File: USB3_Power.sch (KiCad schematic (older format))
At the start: 42 parts, among them U4 NCP1117ST33T3G, U6 CYUSB3014-BZXI

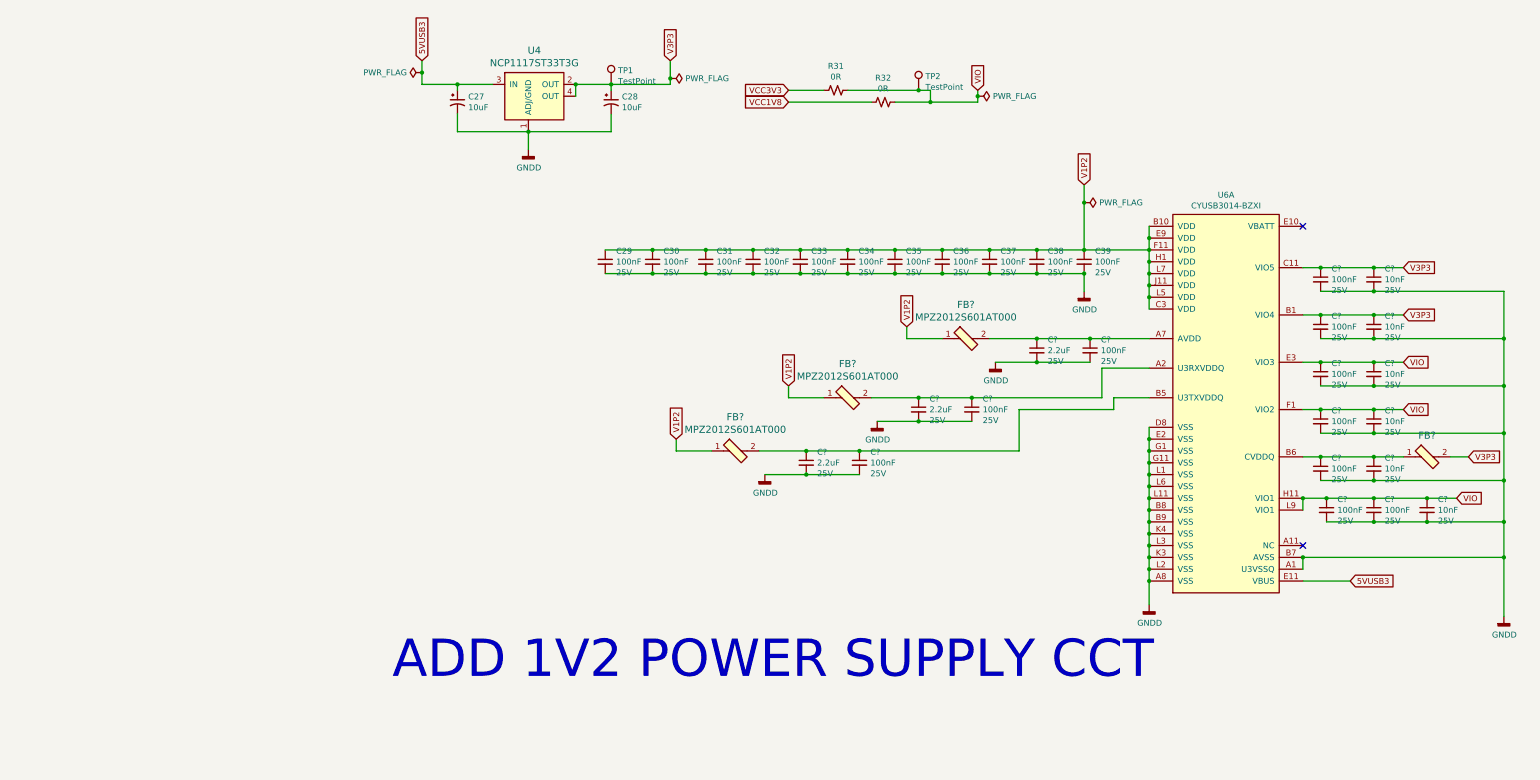
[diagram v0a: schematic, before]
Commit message: Completed USB3 1.2V Added 5V regulator cct partially completed Added BTB connector
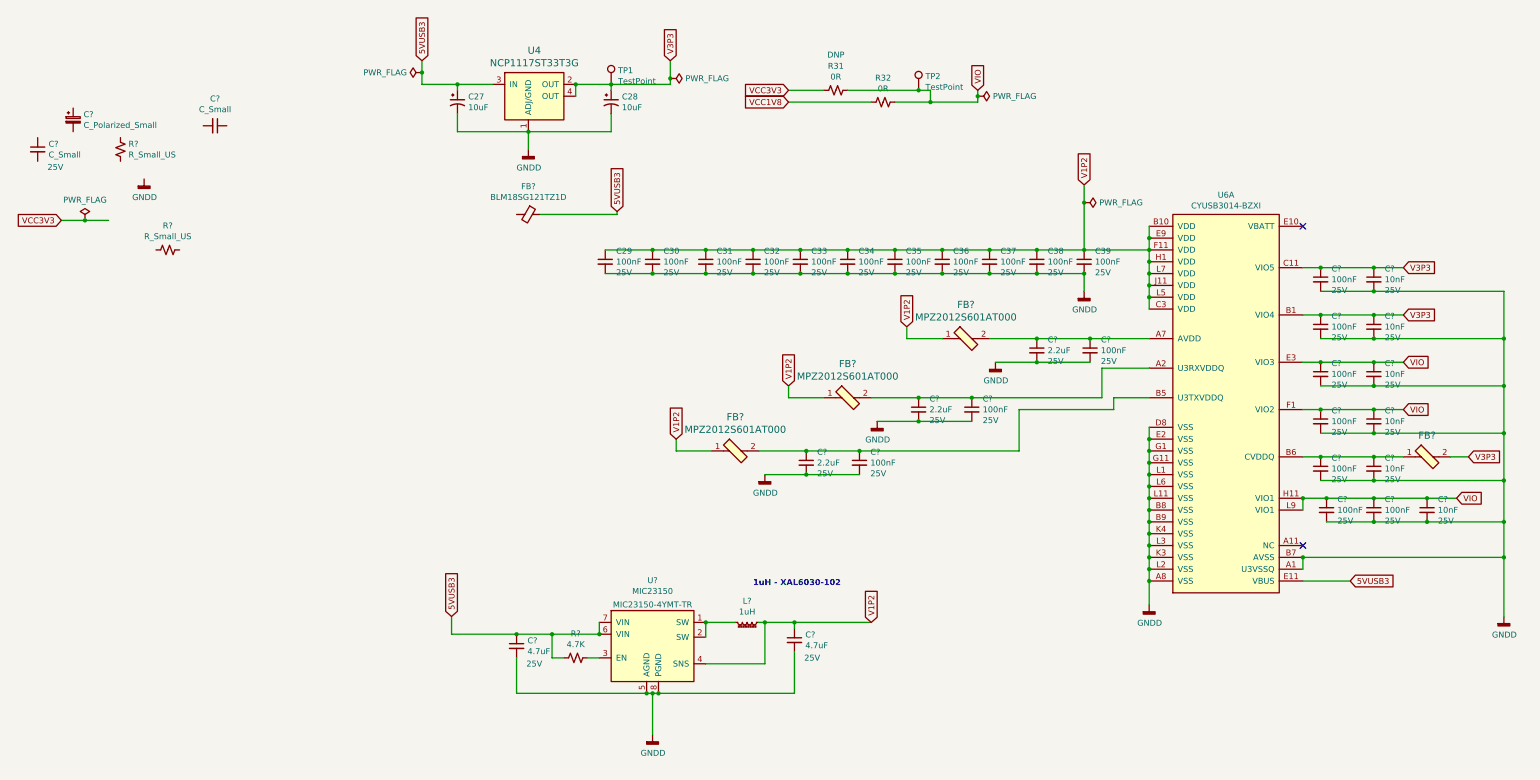
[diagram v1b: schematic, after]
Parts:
- added C?: C_Small, Capacitor_SMD:C_0603_1608Metric_Pad1.08x0.95mm_HandSolder, symbol Device:C_Small
- added C?: C_Polarized_Small, Capacitor_Tantalum_SMD:CP_EIA-1608-10_AVX-L_Pad1.25x1.05mm_HandSolder, symbol Device:C_Polarized_Small
- added C?: C_Small, symbol Device:C_Small
- added C? (x2): 4.7uF, Capacitor_SMD:C_0603_1608Metric_Pad1.08x0.95mm_HandSolder, symbol Device:C_Small
- added FB?: BLM18SG121TZ1D, Inductor_SMD:L_0603_1608Metric_Pad1.05x0.95mm_HandSolder, symbol Device:FerriteBead_Small
- added L?: 1uH, symbol Device:L_Ferrite_Small
- added R? (x2): R_Small_US, Resistor_SMD:R_0603_1608Metric_Pad0.98x0.95mm_HandSolder, symbol Device:R_Small_US
- added R?: 4.7K, Resistor_SMD:R_0603_1608Metric_Pad0.98x0.95mm_HandSolder, symbol Device:R_Small_US
- added U?: MIC23150, GM_TDFN:TDFN-8-2x2mm_P0.5mm, symbol GM_Voltage_Regulators:MIC23150
- R31: DNP (none) -> DNP
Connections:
- net 5VUSB3: now also C?.1, FB?.1, R?.2, U?.6 (VIN), U?.7 (VIN)
- net GNDD: now also C?.2, C?.2, U?.5 (AGND), U?.8 (PGND)
- net V1P2: now also C?.1, L?.1, U?.4 (SNS)
- new net: L?.2, U?.1 (SW), U?.2 (SW)
- new net: R?.1, U?.3 (EN)
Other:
- note added: "1uH - XAL6030-102"
- note removed: "ADD 1V2 POWER SUPPLY CCT"

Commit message: Added USB3 SRAM Added 5V regulator
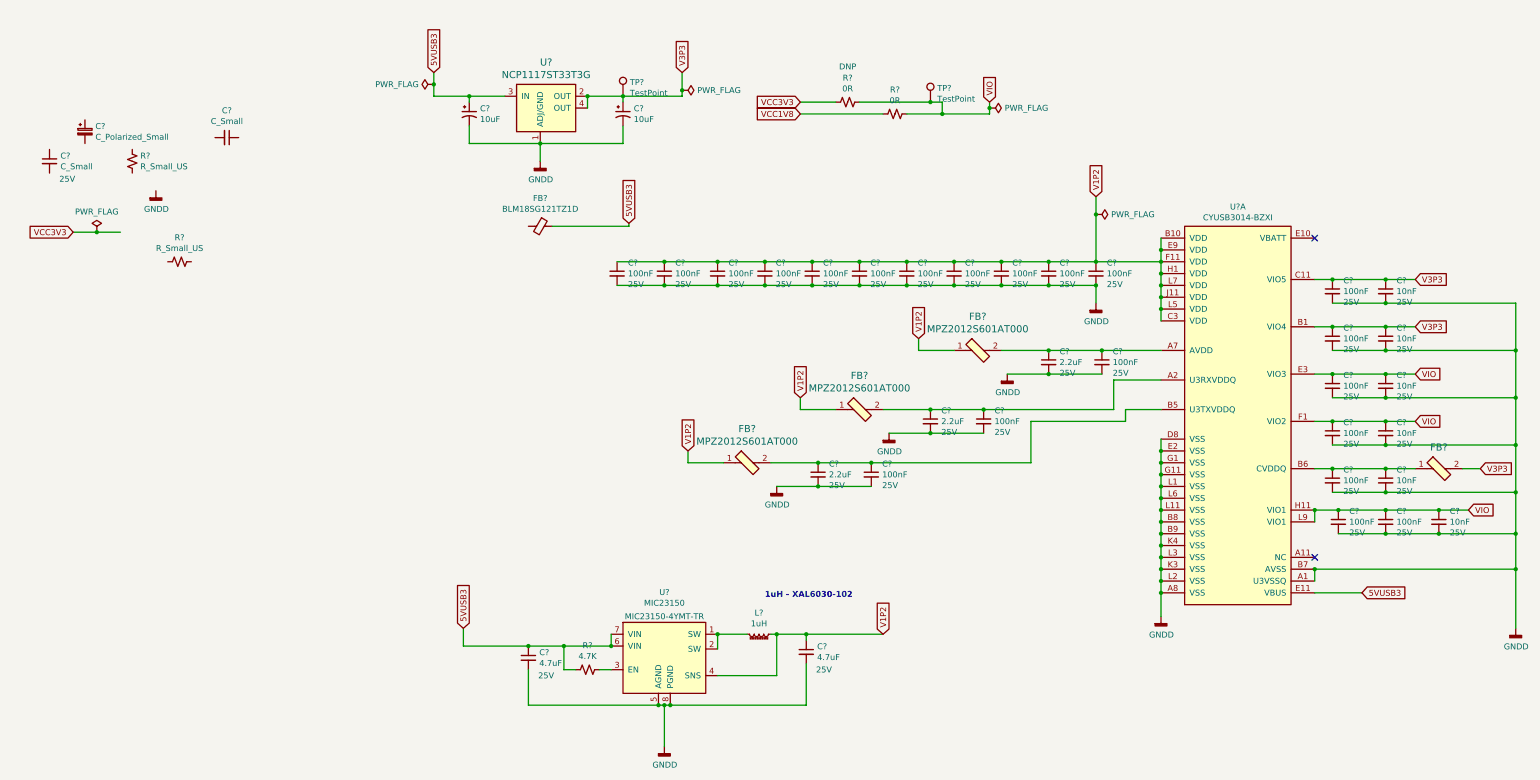
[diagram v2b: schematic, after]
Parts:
- removed C27, C28: 10uF, Capacitor_Tantalum_SMD:CP_EIA-3528-21_Kemet-B_Pad1.50x2.35mm_HandSolder, symbol Device:C_Polarized_Small_US
- removed C29, C30, C31, C32, C33, C34, C35, C36, C37, C38, C39, C? (x10): 100nF, Capacitor_SMD:C_0603_1608Metric_Pad1.08x0.95mm_HandSolder, symbol Device:C_Small
- removed C? (x3): 2.2uF, Capacitor_SMD:C_0603_1608Metric_Pad1.08x0.95mm_HandSolder, symbol Device:C_Small
- removed C? (x6): 10nF, Capacitor_SMD:C_0603_1608Metric_Pad1.08x0.95mm_HandSolder, symbol Device:C_Small
- removed C?: C_Small, Capacitor_SMD:C_0603_1608Metric_Pad1.08x0.95mm_HandSolder, symbol Device:C_Small
- removed C?: C_Polarized_Small, Capacitor_Tantalum_SMD:CP_EIA-1608-10_AVX-L_Pad1.25x1.05mm_HandSolder, symbol Device:C_Polarized_Small
- removed C?: C_Small, symbol Device:C_Small
- removed C? (x2): 4.7uF, Capacitor_SMD:C_0603_1608Metric_Pad1.08x0.95mm_HandSolder, symbol Device:C_Small
- removed FB? (x4): MPZ2012S601AT000, digikey-footprints:0805, symbol dk_Ferrite-Beads-and-Chips:MPZ2012S601AT000
- removed FB?: BLM18SG121TZ1D, Inductor_SMD:L_0603_1608Metric_Pad1.05x0.95mm_HandSolder, symbol Device:FerriteBead_Small
- removed L?: 1uH, symbol Device:L_Ferrite_Small
- removed R31, R32: 0R, Resistor_SMD:R_0603_1608Metric_Pad0.98x0.95mm_HandSolder, symbol Device:R_Small_US
- removed R? (x2): R_Small_US, Resistor_SMD:R_0603_1608Metric_Pad0.98x0.95mm_HandSolder, symbol Device:R_Small_US
- removed R?: 4.7K, Resistor_SMD:R_0603_1608Metric_Pad0.98x0.95mm_HandSolder, symbol Device:R_Small_US
- removed TP1, TP2: TestPoint, TestPoint:TestPoint_Pad_2.0x2.0mm, symbol Connector:TestPoint
- removed U4: NCP1117ST33T3G, digikey-footprints:SOT-223, symbol dk_PMIC-Voltage-Regulators-Linear:NCP1117ST33T3G
- removed U6: CYUSB3014-BZXI, Package_BGA:BGA121C80P11X11_1000X1000X120, symbol GM_Microcontrollers:CYUSB3014-BZXI
- removed U?: MIC23150, GM_TDFN:TDFN-8-2x2mm_P0.5mm, symbol GM_Voltage_Regulators:MIC23150
- added C? (x2): 4.7uF, Capacitor_SMD:C_0603_1608Metric_Pad1.08x0.95mm_HandSolder, symbol Device:C_Small
- added C?: C_Small, symbol Device:C_Small
- added C?: C_Polarized_Small, Capacitor_Tantalum_SMD:CP_EIA-1608-10_AVX-L_Pad1.25x1.05mm_HandSolder, symbol Device:C_Polarized_Small
- added C?: C_Small, Capacitor_SMD:C_0603_1608Metric_Pad1.08x0.95mm_HandSolder, symbol Device:C_Small
- added C? (x21): 100nF, Capacitor_SMD:C_0603_1608Metric_Pad1.08x0.95mm_HandSolder, symbol Device:C_Small
- added C? (x6): 10nF, Capacitor_SMD:C_0603_1608Metric_Pad1.08x0.95mm_HandSolder, symbol Device:C_Small
- added C? (x3): 2.2uF, Capacitor_SMD:C_0603_1608Metric_Pad1.08x0.95mm_HandSolder, symbol Device:C_Small
- added C? (x2): 10uF, Capacitor_Tantalum_SMD:CP_EIA-3528-21_Kemet-B_Pad1.50x2.35mm_HandSolder, symbol Device:C_Polarized_Small_US
- added FB?: BLM18SG121TZ1D, Inductor_SMD:L_0603_1608Metric_Pad1.05x0.95mm_HandSolder, symbol Device:FerriteBead_Small
- added FB? (x4): MPZ2012S601AT000, digikey-footprints:0805, symbol dk_Ferrite-Beads-and-Chips:MPZ2012S601AT000
- added L?: 1uH, symbol Device:L_Ferrite_Small
- added R?: 4.7K, Resistor_SMD:R_0603_1608Metric_Pad0.98x0.95mm_HandSolder, symbol Device:R_Small_US
- added R? (x2): R_Small_US, Resistor_SMD:R_0603_1608Metric_Pad0.98x0.95mm_HandSolder, symbol Device:R_Small_US
- added R? (x2): 0R, Resistor_SMD:R_0603_1608Metric_Pad0.98x0.95mm_HandSolder, symbol Device:R_Small_US
- added TP? (x2): TestPoint, TestPoint:TestPoint_Pad_2.0x2.0mm, symbol Connector:TestPoint
- added U?: MIC23150, GM_TDFN:TDFN-8-2x2mm_P0.5mm, symbol GM_Voltage_Regulators:MIC23150
- added U?: NCP1117ST33T3G, digikey-footprints:SOT-223, symbol dk_PMIC-Voltage-Regulators-Linear:NCP1117ST33T3G
- added U?: CYUSB3014-BZXI, Package_BGA:BGA121C80P11X11_1000X1000X120, symbol GM_Microcontrollers:CYUSB3014-BZXI
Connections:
- net 5VUSB3: now also C?.1, C?.1, FB?.1, R?.2, U?.3 (IN), U?.6 (VIN), U?.7 (VIN), U?.E11 (VBUS)
- net GNDD: now also C?.2, C?.2, C?.2, C?.2, C?.2, C?.2, C?.2, C?.2, C?.2, C?.2, C?.2, C?.2, C?.2, C?.2, C?.2, C?.2, C?.2, C?.2, C?.2, C?.2, C?.2, C?.2, C?.2, C?.2, C?.2, C?.2, C?.2, C?.2, C?.2, C?.2, C?.2, C?.2, C?.2, C?.2, U?.1 (ADJ/GND), U?.5 (AGND), U?.8 (PGND), U?.A1 (U3VSSQ), U?.A8 (VSS), U?.B7 (AVSS), U?.B8 (VSS), U?.B9 (VSS), U?.D8 (VSS), U?.E2 (VSS), U?.G1 (VSS), U?.G11 (VSS), U?.K3 (VSS), U?.K4 (VSS), U?.L1 (VSS), U?.L11 (VSS), U?.L2 (VSS), U?.L3 (VSS), U?.L6 (VSS)
- net V1P2: now also C?.1, C?.1, C?.1, C?.1, C?.1, C?.1, C?.1, C?.1, C?.1, C?.1, C?.1, C?.1, FB?.1, FB?.1, FB?.1, L?.1, U?.4 (SNS), U?.B10 (VDD), U?.C3 (VDD), U?.E9 (VDD), U?.F11 (VDD), U?.H1 (VDD), U?.J11 (VDD), U?.L5 (VDD), U?.L7 (VDD)
- net V3P3: now also C?.1, C?.1, C?.1, C?.1, C?.1, FB?.2, TP?.1, U?.2 (OUT), U?.4 (OUT), U?.B1 (VIO4), U?.C11 (VIO5)
- net VCC1V8: now also R?.2
- net VCC3V3: now also R?.2
- net VIO: now also C?.1, C?.1, C?.1, C?.1, C?.1, C?.1, C?.1, R?.1, R?.1, TP?.1, U?.E3 (VIO3), U?.F1 (VIO2), U?.H11 (VIO1), U?.L9 (VIO1)
- new net: L?.2, U?.1 (SW), U?.2 (SW)
- new net: R?.1, U?.3 (EN)
- new net: C?.1, C?.1, FB?.1, U?.B6 (CVDDQ)
- new net: C?.1, C?.1, FB?.2, U?.B5 (U3TXVDDQ)
- new net: C?.1, C?.1, FB?.2, U?.A2 (U3RXVDDQ)
- new net: C?.1, C?.1, FB?.2, U?.A7 (AVDD)

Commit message: Added USB3 type B connector Added ESD protection to the same sheet
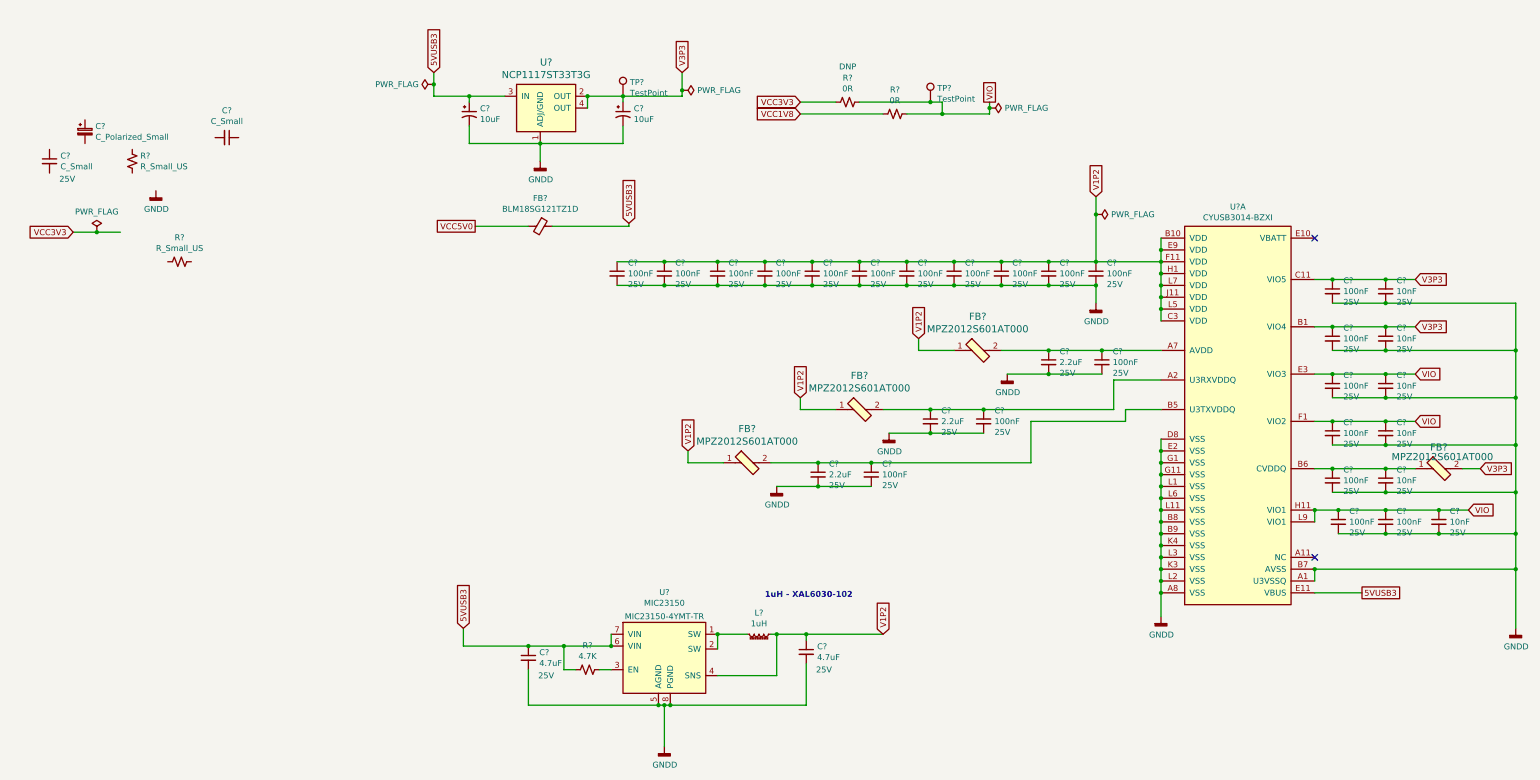
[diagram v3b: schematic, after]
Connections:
- net VCC5V0: now reaches FB?.2
